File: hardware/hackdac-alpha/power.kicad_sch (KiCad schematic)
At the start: 51 parts, among them J10 HOLE, J11 HOLE, J12 EXT POWER, J5 EXT LEDS, J6 HOLE, J7 HOLE, J8 HOLE, J9 HOLE, P3 P20, P4 P28, Q6 IRLML2244, U14 TPS61170DRVR, U15 TPS63700DRCT, U3 TLE2082, U7 74LVC1G07

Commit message: V3 PCB WIP
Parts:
- J6: renamed from J5; footprint (none) -> Connector_Molex:Molex_PicoBlade_53047-0410_1x04_P1.25mm_Vertical
- R49: renamed from R47; footprint (none) -> Resistor_SMD:R_0603_1608Metric
- R51: renamed from R48; footprint (none) -> Resistor_SMD:R_0603_1608Metric
- R52: renamed from R49; footprint (none) -> Resistor_SMD:R_0603_1608Metric
- R54: renamed from R45; footprint (none) -> Resistor_SMD:R_0603_1608Metric
- U10: renamed from U7; footprint (none) -> Package_TO_SOT_SMD:SOT-23-5
- renumbered C66 to C65, C67 to C66, C76 to C67, C77 to C68, C78 to C69, C79 to C70, C80 to C71, C81 to C72, C82 to C73, C83 to C74, C84 to C75, C85 to C76, C86 to C77, C87 to C78, D6 to D5, D7 to D6, D5 to D7, J8 to J10, J9 to J11, J10 to J12, J11 to J13, J12 to J7, J6 to J8, J7 to J9, L14 to L11, L15 to L12, L18 to L13, L19 to L14, P4 to P3, P3 to P4, Q6 to Q7, R53 to R48, R46 to R50, R54 to R53, R58 to R55, R59 to R56, R60 to R57, R61 to R58, R62 to R59, R63 to R60, U14 to U11, U15 to U12
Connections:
- net +5V: now also J7.3 (Pin_3); no longer J7.1 (Pin_1)
- net -5V: now also J7.1 (Pin_1); no longer J7.3 (Pin_3)

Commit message: V3 PCB WIP
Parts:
- renumbered R50 to R49, R53 to R50, R49 to R51, R51 to R52, R54 to R53, R52 to R54
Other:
- moved on the sheet: J6, R51, R52, R54

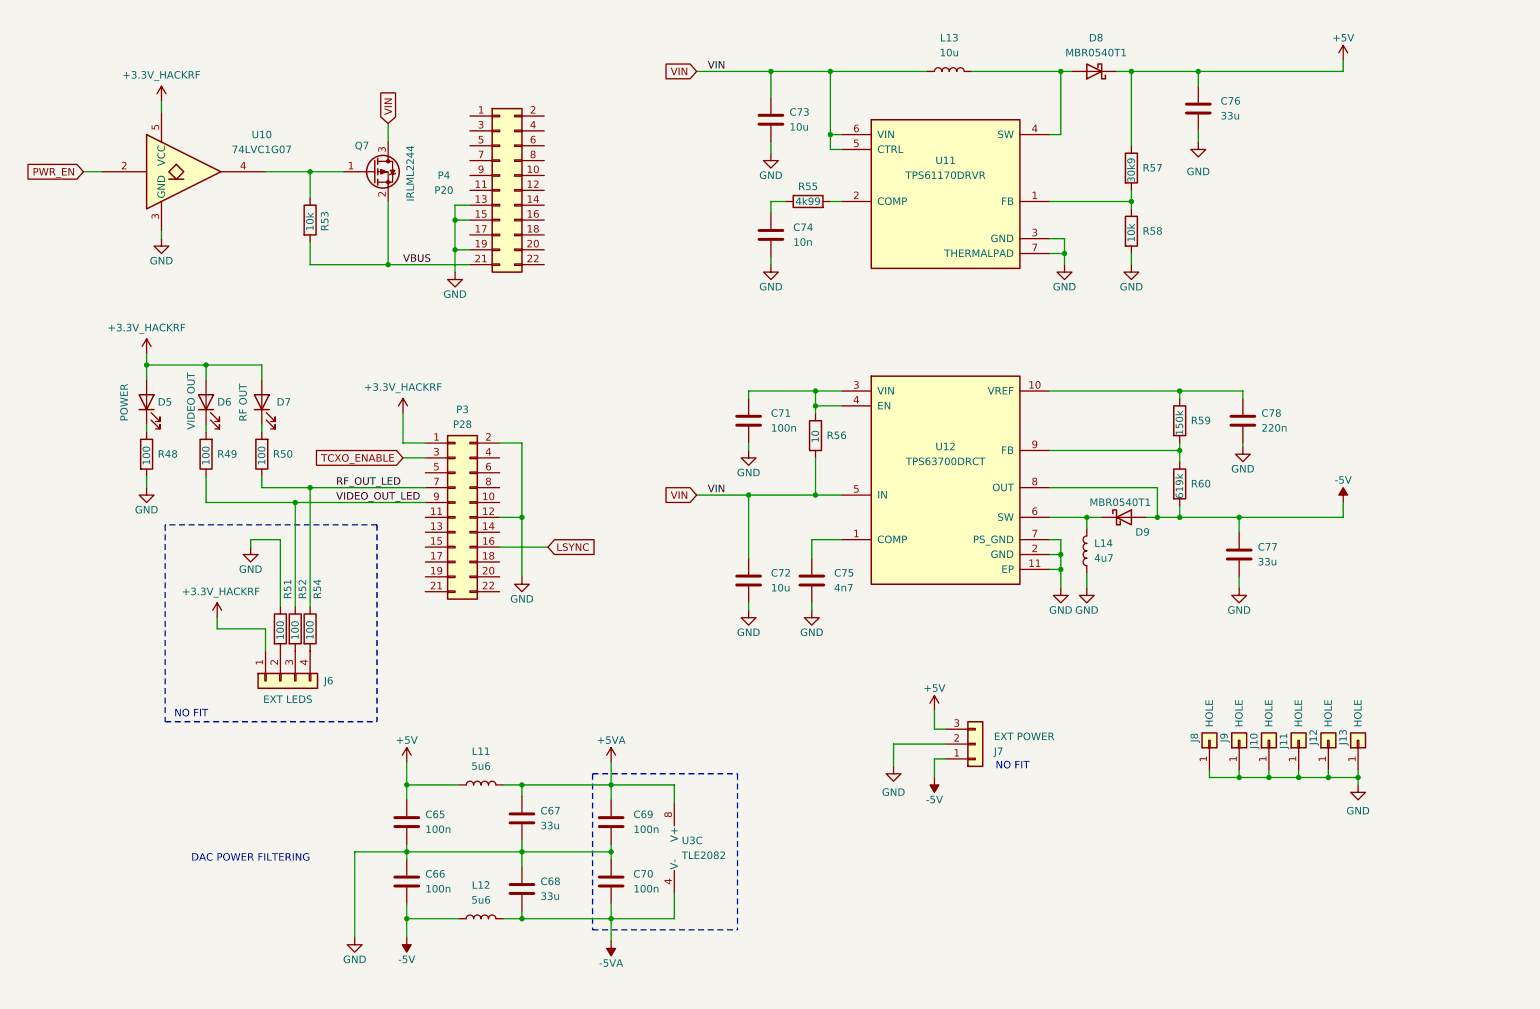
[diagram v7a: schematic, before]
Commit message: Optional caps for DAC supply
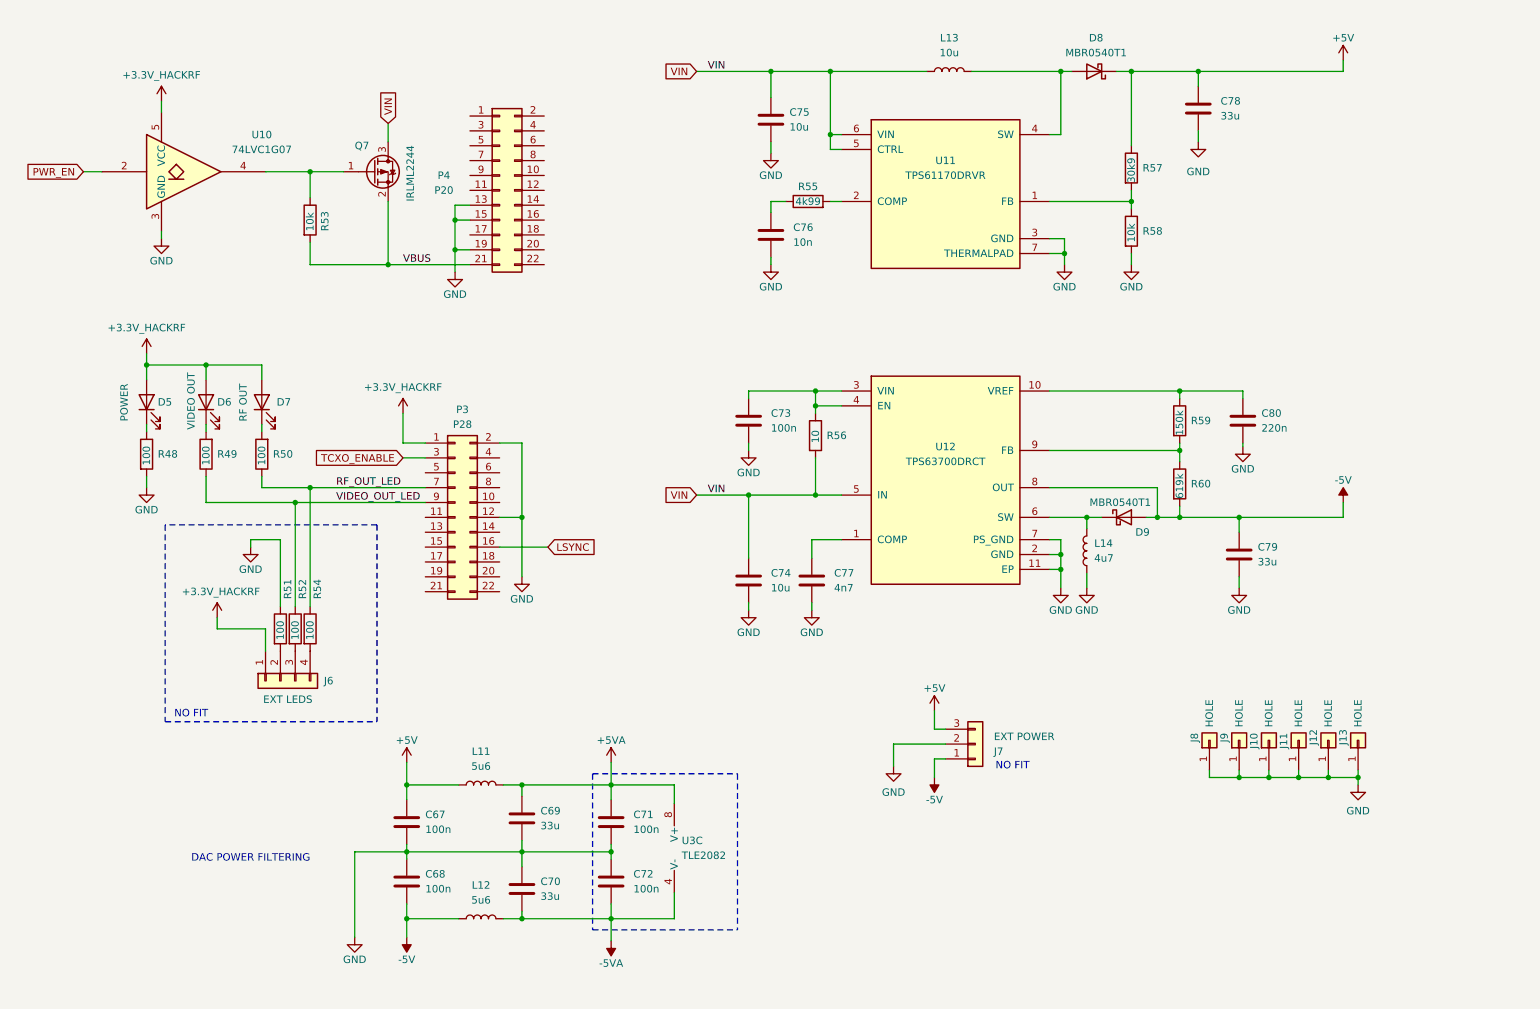
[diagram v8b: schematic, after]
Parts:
- renumbered C65 to C67, C66 to C68, C67 to C69, C68 to C70, C69 to C71, C70 to C72, C71 to C73, C72 to C74, C73 to C75, C74 to C76, C75 to C77, C76 to C78, C77 to C79, C78 to C80
